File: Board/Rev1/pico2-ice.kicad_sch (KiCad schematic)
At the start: 122 parts, among them J1 USB_C_Receptacle_USB2.0, J2 Conn_02x20_Odd_Even, J3 Conn_02x20_Odd_Even, J5 BM03B-SRSS-TB, J6 Conn_01x22_MountingPin, SW1 CS1213AGF260, SW2 CS1213AGF260, U1 NCP115AMX120TCG, U2 W25Q32JVSSIQ, U3 RP2350_80QFN, U4 TL431DBZ, U5 APS6404L-3SQN-SN, U6 ICE40UP5K-SG48ITR, U8 W25Q32JVSSIQ, U9 NCP115AMX330TCG, Y1 ABM8-272-T3

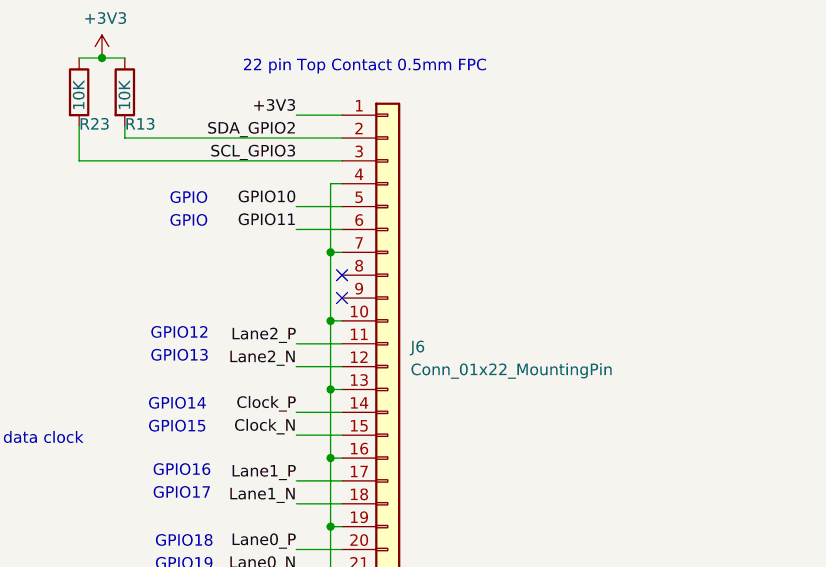
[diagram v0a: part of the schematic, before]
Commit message: Bugfixes for silkscreen PMOD, added DONE, unconnected RP22 pins, layout not yet complete
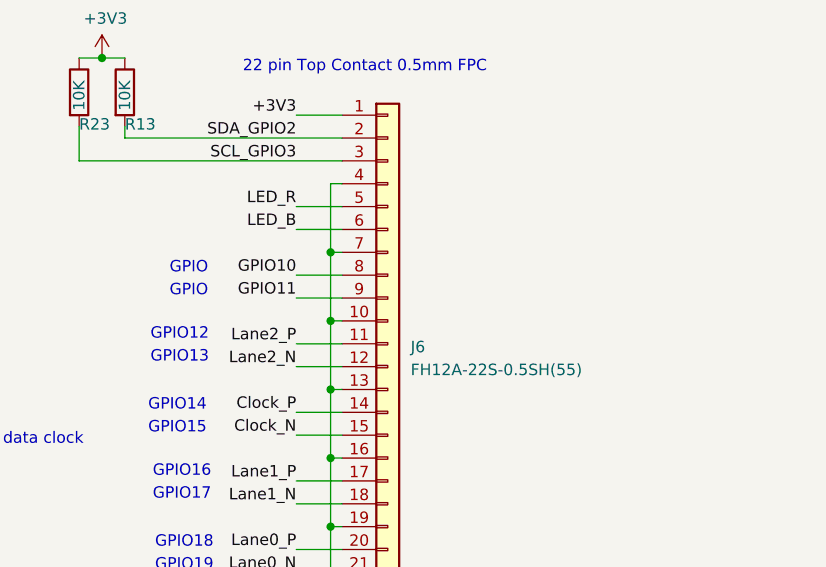
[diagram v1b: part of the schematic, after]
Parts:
- J6: value Conn_01x22_MountingPin -> FH12A-22S-0.5SH(55)
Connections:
- net GPIO10: now also J6.8 (Pin_8); no longer J6.5 (Pin_5)
- net GPIO11: now also J6.9 (Pin_9); no longer J6.6 (Pin_6)
- net LED_B: now also J6.6 (Pin_6)
- net LED_R: now also J6.5 (Pin_5)
- no-connect marks 4 -> 2
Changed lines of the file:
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@@
 	)
 	(no_connect
-		(at 228.6 207.01)
-	)
-	(no_connect
 		(at 41.91 55.88)
 	)
@@
 		(at 41.91 58.42)
 	)
-	(no_connect
-		(at 228.6 204.47)
-	)
 	(wire
 		(pts
@@
 	(wire
 		(pts
+			(xy 223.52 204.47) (xy 228.6 204.47)
+		)
+		(stroke
+			(width 0)
+			(type default)
+		)
+	)
+	(wire
+		(pts
 			(xy 497.84 74.93) (xy 494.03 74.93)
 		)
@@
 	(wire
 		(pts
+			(xy 223.52 207.01) (xy 228.6 207.01)
+		)
+		(stroke
+			(width 0)
+			(type default)
+		)
+	)
+	(wire
+		(pts
 			(xy 394.97 177.8) (xy 388.62 177.8)
 		)
@@
 		)
 	)
+	(text "GPIO"
+		(exclude_from_sim no)
+		(at 211.582 206.248 0)
+		(effects
+			(font
+				(size 1.27 1.27)
+			)
+		)
+	)
 	(text "SRAM"
 		(exclude_from_sim no)
@@
 		)
 	)
+	(text "GPIO"
+		(exclude_from_sim no)
+		(at 211.582 203.708 0)
+		(effects
+			(font
+				(size 1.27 1.27)
+			)
+		)
+	)
 	(text "iCE-Pico PMOD"
 		(exclude_from_sim no)
@@
 		)
 	)
-	(text "GPIO"
-		(exclude_from_sim no)
-		(at 211.582 196.088 0)
-		(effects
-			(font
-				(size 1.27 1.27)
-			)
-		)
-	)
 	(text "GPIO13"
 		(exclude_from_sim no)
@@
 		)
 	)
-	(text "GPIO"
-		(exclude_from_sim no)
-		(at 211.582 198.628 0)
-		(effects
-			(font
-				(size 1.27 1.27)
-			)
-		)
-	)
 	(text "Note: \nAdd DNF if the Flash is\nreplaced with an SRAM."
 		(exclude_from_sim no)
@@
 		)
 	)
+	(label "LED_R"
+		(at 223.52 196.85 180)
+		(fields_autoplaced yes)
+		(effects
+			(font
+				(size 1.27 1.27)
+			)
+			(justify right bottom)
+		)
+	)
 	(label "ICE_SO"
 		(at 513.715 41.91 0)
@@
 		)
 	)
-	(label "GPIO11"
-		(at 223.52 199.39 180)
-		(fields_autoplaced yes)
-		(effects
-			(font
-				(size 1.27 1.27)
-			)
-			(justify right bottom)
-		)
-	)
 	(label "QSPI_SCLK"
 		(at 63.5 194.31 0)
@@
 		)
 	)
+	(label "GPIO11"
+		(at 223.52 207.01 180)
+		(fields_autoplaced yes)
+		(effects
+			(font
+				(size 1.27 1.27)
+			)
+			(justify right bottom)
+		)
+	)
 	(label "Lane1_P"
 		(at 148.59 208.28 0)
@@
 		)
 	)
-	(label "GPIO10"
-		(at 223.52 196.85 180)
-		(fields_autoplaced yes)
-		(effects
-			(font
-				(size 1.27 1.27)
-			)
-			(justify right bottom)
-		)
-	)
 	(label "PICO_PMOD_A3"
 		(at 148.59 248.92 0)
@@
 		)
 	)
+	(label "LED_B"
+		(at 223.52 199.39 180)
+		(fields_autoplaced yes)
+		(effects
+			(font
+				(size 1.27 1.27)
+			)
+			(justify right bottom)
+		)
+	)
 	(label "PICO_PMOD_B1"
 		(at 148.59 261.62 0)
@@
 		)
 	)
+	(label "GPIO10"
+		(at 223.52 204.47 180)
+		(fields_autoplaced yes)
+		(effects
+			(font
+				(size 1.27 1.27)
+			)
+			(justify right bottom)
+		)
+	)
 	(label "ICE_18"
 		(at 148.59 236.22 0)
@@
 			)
 		)
-		(property "Value" "Conn_01x22_MountingPin"
+		(property "Value" "FH12A-22S-0.5SH(55)"
 			(at 236.22 214.9855 0)
 			(effects

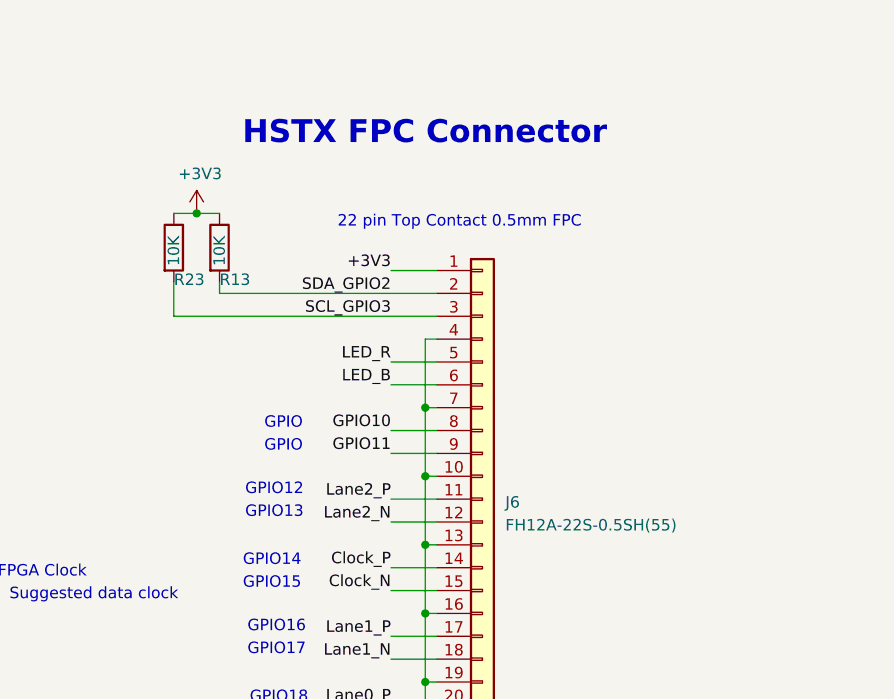
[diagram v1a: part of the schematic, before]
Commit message: Changed MPN on the FPC and updated datasheet link to the PSRAM
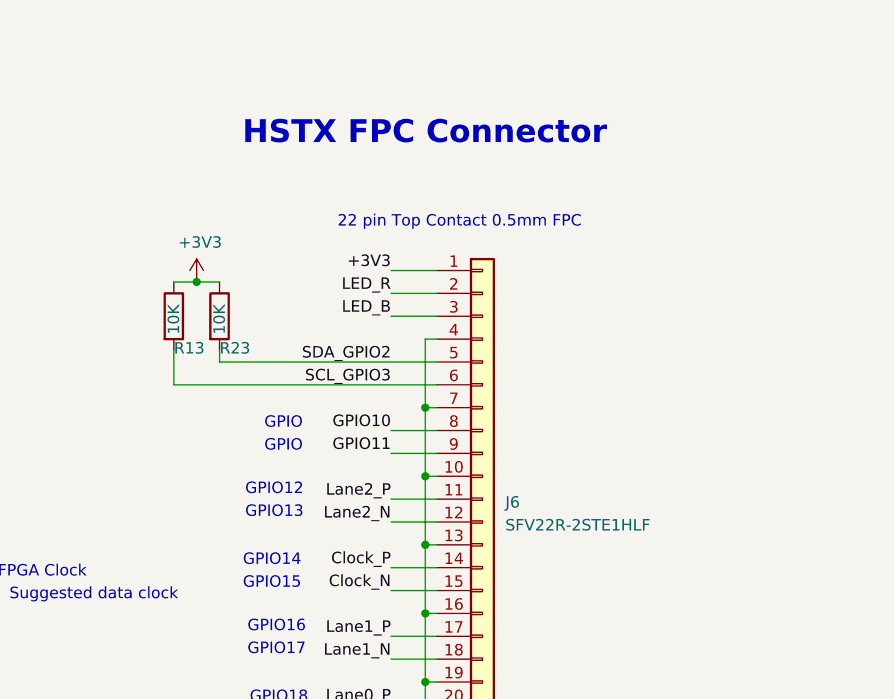
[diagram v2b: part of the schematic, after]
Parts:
- J6: value FH12A-22S-0.5SH(55) -> SFV22R-2STE1HLF
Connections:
- net LED_B: now also J6.3 (Pin_3); no longer J6.6 (Pin_6)
- net LED_R: now also J6.2 (Pin_2); no longer J6.5 (Pin_5)
- net SCL_GPIO3: now also J6.6 (Pin_6), R13.2; no longer J6.3 (Pin_3), R23.2
- net SDA_GPIO2: now also J6.5 (Pin_5), R23.2; no longer J6.2 (Pin_2), R13.2

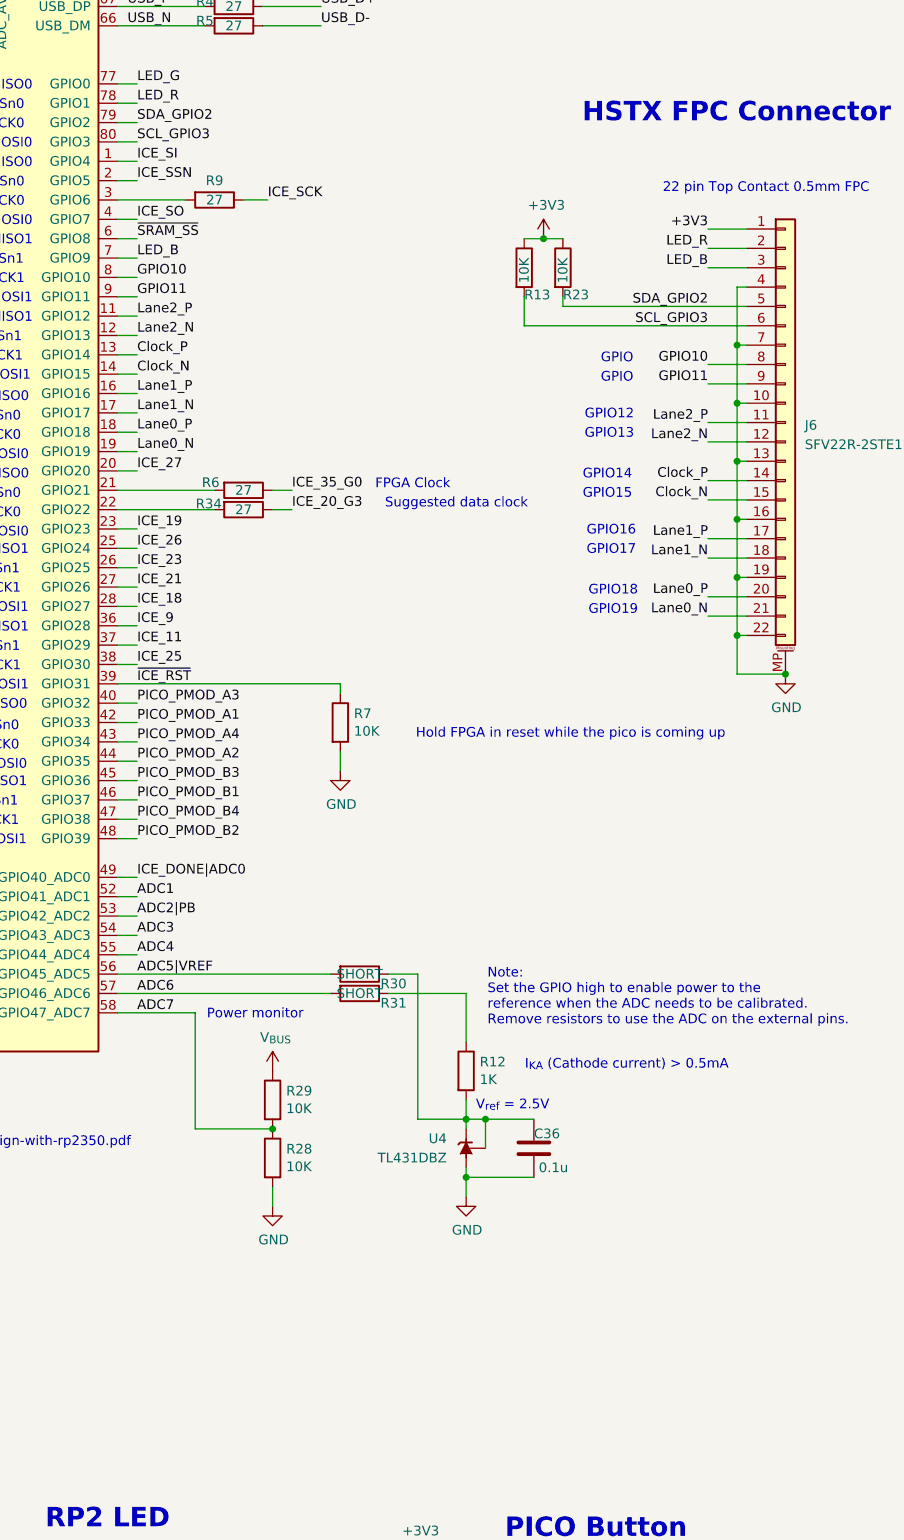
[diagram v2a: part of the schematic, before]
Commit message: Added voltage monitor
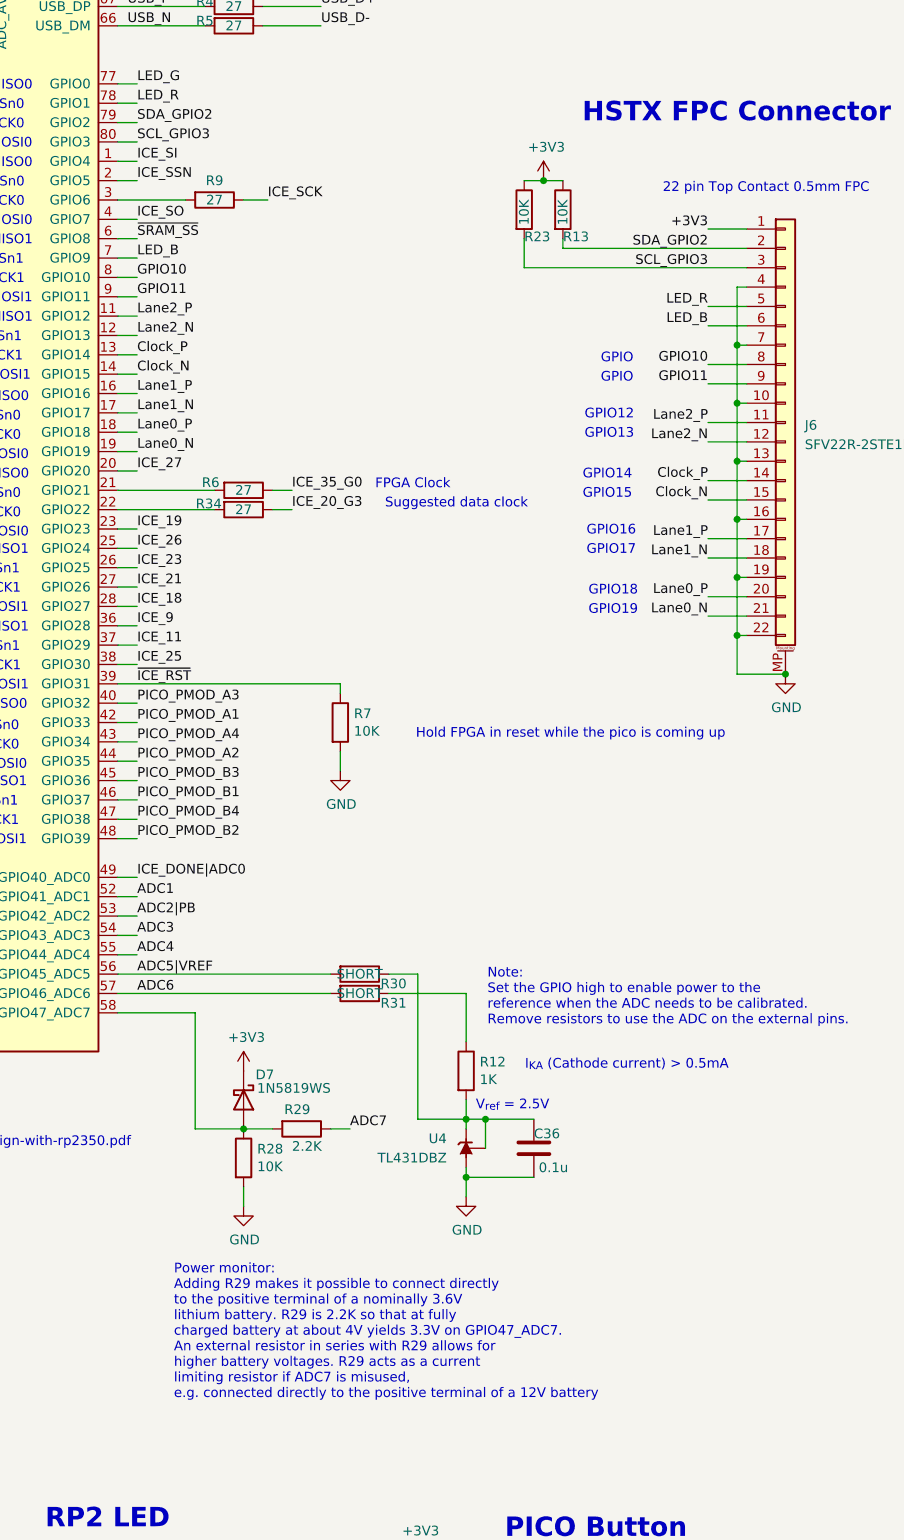
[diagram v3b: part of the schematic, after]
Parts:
- added D7: 1N5819WS, Diode_SMD:D_SOD-323, symbol Device:D_Schottky
- R29: value 10K -> 2.2K
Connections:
- net +3V3: now also D7.1 (K)
- net ADC7: now also R29.1; no longer R28.1, R29.2, U3.58 (GPIO47_ADC7)
- net LED_B: now also J6.6 (Pin_6); no longer J6.3 (Pin_3)
- net LED_R: now also J6.5 (Pin_5); no longer J6.2 (Pin_2)
- net SCL_GPIO3: now also J6.3 (Pin_3), R23.2; no longer J6.6 (Pin_6), R13.2
- net SDA_GPIO2: now also J6.2 (Pin_2), R13.2; no longer J6.5 (Pin_5), R23.2
- net V_{BUS}: no longer R29.1
- new net: D7.2 (A), R28.1, R29.2, U3.58 (GPIO47_ADC7)
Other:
- note added: "Power monitor: Adding R29 makes it possible to connect directly to the positive terminal of a nominally 3.6V lithium battery. R29 is 2.2K so that at fully charged battery at about 4V yields 3.3V on GPIO47_ADC7. An external resistor in series with R29 allows for higher battery voltages. R29 acts as a current limiting resistor if ADC7 is misused, e.g. connected directly to the positive terminal of 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"
- note removed: "Power monitor"
- moved on the sheet: R28, R29
